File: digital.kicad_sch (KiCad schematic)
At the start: 23 parts, among them J10 DISP, J11 ENC1, J12 ENC2, J8 SWD, U8 STM32G431RBT6, Y1 8MHz

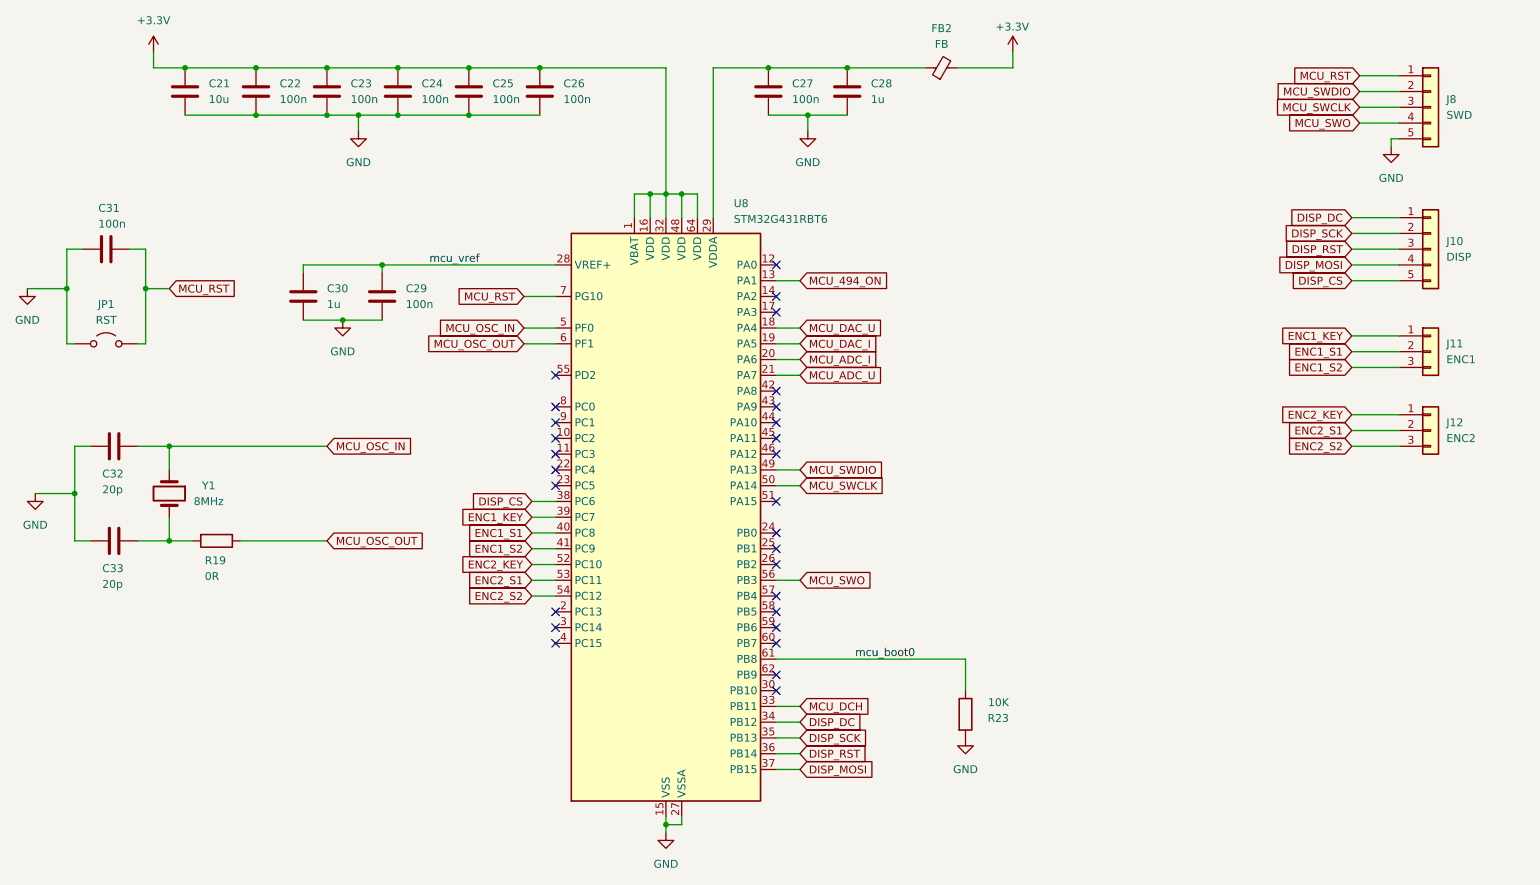
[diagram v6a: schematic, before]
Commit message: added fan control and ds18b20 to the schematic
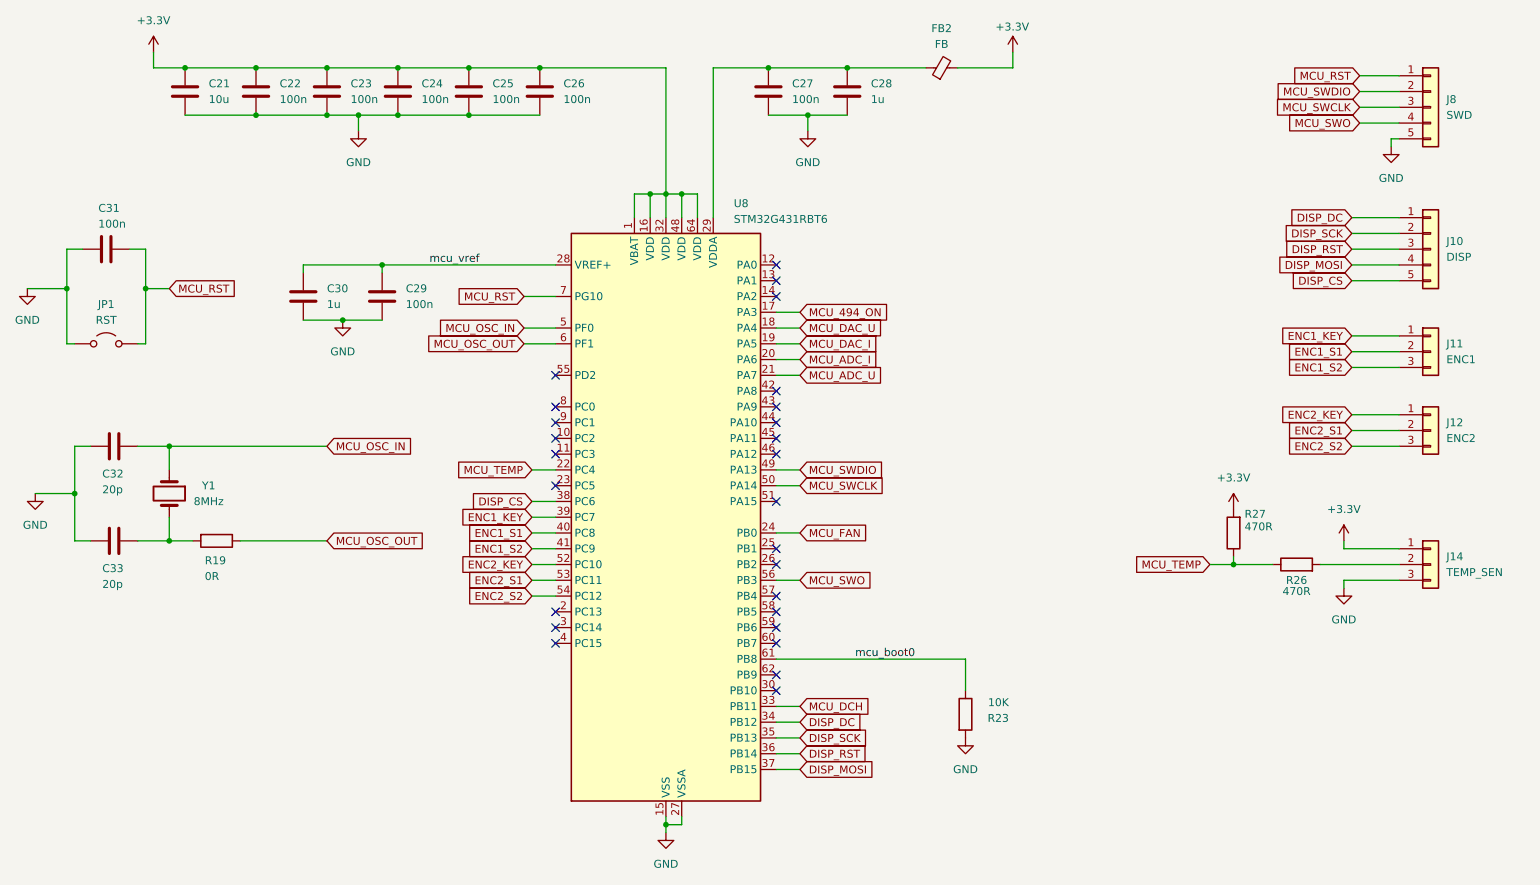
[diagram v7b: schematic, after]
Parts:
- added J14: TEMP_SEN, Connector_PinHeader_2.54mm:PinHeader_1x03_P2.54mm_Vertical, symbol Connector_Generic:Conn_01x03
- added R26, R27: 470R, Resistor_SMD:R_1206_3216Metric_Pad1.30x1.75mm_HandSolder, symbol Device:R
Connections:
- net +3.3V: now also J14.1 (Pin_1), R27.2
- net GND: now also J14.3 (Pin_3)
- net MCU_494_ON: now also U8.17 (PA3); no longer U8.13 (PA1)
- net MCU_TEMP: now reaches U8.22 (PC4)
- net MCU_TEMP: now also R26.1, R27.1
- net MCU_FAN: now reaches U8.24 (PB0)
- new net: J14.2 (Pin_2), R26.2
- no-connect marks 28 -> 26

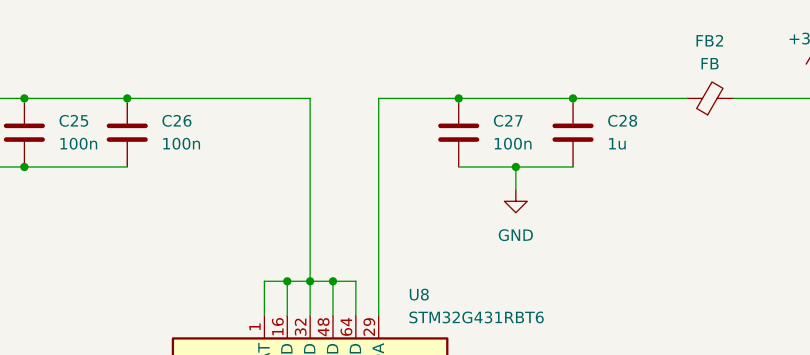
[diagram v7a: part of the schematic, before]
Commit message: fan and temp sensor tracing
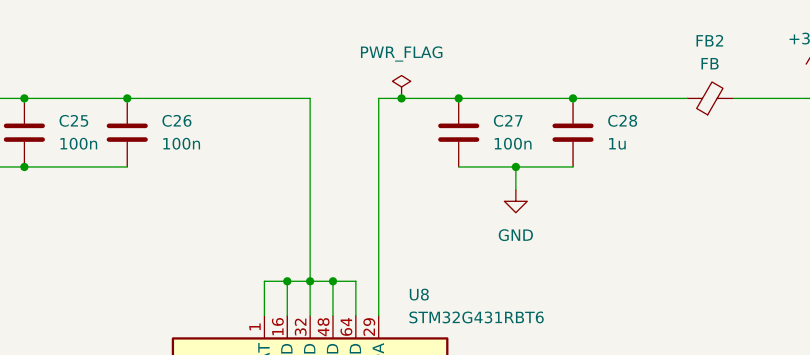
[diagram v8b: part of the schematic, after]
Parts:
- J14: footprint Connector_PinHeader_2.54mm:PinHeader_1x03_P2.54mm_Vertical -> Connector_JST:JST_XH_B3B-XH-A_1x03_P2.50mm_Vertical
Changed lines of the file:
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@@
 	)
 	(junction
+		(at 137.16 25.4)
+		(diameter 0)
+		(color 0 0 0 0)
+	)
+	(junction
 		(at 95.25 33.02)
 		(diameter 0)
@@
 	(wire
 		(pts
+			(xy 137.16 25.4) (xy 143.51 25.4)
+		)
+		(stroke
+			(width 0)
+			(type default)
+		)
+	)
+	(wire
+		(pts
 			(xy 31.75 86.36) (xy 31.75 93.98)
 		)
@@
 	(wire
 		(pts
-			(xy 134.62 25.4) (xy 143.51 25.4)
+			(xy 134.62 25.4) (xy 137.16 25.4)
 		)
 		(stroke
@@
 	)
 	(symbol
+		(lib_id "power:PWR_FLAG")
+		(at 137.16 25.4 0)
+		(unit 1)
+		(exclude_from_sim no)
+		(in_bom yes)
+		(on_board yes)
+		(dnp no)
+		(fields_autoplaced yes)
+		(property "Reference" "#FLG06"
+			(at 137.16 23.495 0)
+			(effects
+				(font
+					(size 1.27 1.27)
+				)
+				(hide yes)
+			)
+		)
+		(property "Value" "PWR_FLAG"
+			(at 137.16 20.32 0)
+			(effects
+				(font
+					(size 1.27 1.27)
+				)
+			)
+		)
+		(property "Footprint" ""
+			(at 137.16 25.4 0)
+			(effects
+				(font
+					(size 1.27 1.27)
+				)
+				(hide yes)
+			)
+		)
+		(property "Datasheet" "~"
+			(at 137.16 25.4 0)
+			(effects
+				(font
+					(size 1.27 1.27)
+				)
+				(hide yes)
+			)
+		)
+		(property "Description" "Special symbol for telling ERC where power comes from"
+			(at 137.16 25.4 0)
+			(effects
+				(font
+					(size 1.27 1.27)
+				)
+				(hide yes)
+			)
+		)
+		(pin "1"
+		)
+		(instances
+			(project "RPS_ATX"
+				(path "/485c2fed-5176-4ba8-b79d-ac7eddb44491/422ff71a-ee59-41d3-a8e4-e6d2465802f7"
+					(reference "#FLG06")
+					(unit 1)
+				)
+			)
+		)
+	)
+	(symbol
 		(lib_id "power:+3.3VA")
 		(at 182.88 22.86 0)
@@
 			)
 		)
-		(property "Footprint" "Connector_PinHeader_2.54mm:PinHeader_1x03_P2.54mm_Vertical"
+		(property "Footprint" "Connector_JST:JST_XH_B3B-XH-A_1x03_P2.50mm_Vertical"
 			(at 250.19 105.41 0)
 			(effects
